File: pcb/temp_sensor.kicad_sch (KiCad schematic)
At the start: 4 parts, among them SW3 PTS810

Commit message: add top level schem and cleanup
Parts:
- removed C15: 100n, Capacitor_SMD:C_0402_1005Metric, symbol Device:C
- removed R7, R8: 10k, Resistor_SMD:R_0402_1005Metric, symbol Device:R
- removed SW3: PTS810, Button_Switch_SMD:SW_SPST_PTS810, symbol Switch:SW_SPST
- added C23: 0.1u, symbol Device:C
- added R39: 4.7k, symbol Device:R
- added U6: LM75ADP, symbol Sensor_Temperature:LM75B
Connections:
- net +3.3V: now also C23.1, R39.2, U6.8 (+Vs)
- net GND: now also C23.2, U6.4 (GND), U6.5 (A2), U6.6 (A1), U6.7 (A0)
- new net I2C.SCL: U6.2 (SCL)
- new net I2C.SDA: U6.1 (SDA)
- new net temp_int: R39.1, U6.3 (O.S.)
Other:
- company: RoboJackets Electrical Training -> (none)
- title: Debounced Button -> Temperature Sensor

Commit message: cleanup routing
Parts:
- removed R39: 4.7k, symbol Device:R
- added R12: 4.7k, symbol Device:R
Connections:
- net +3.3V: now also R12.1
- net temp_int: no longer names the net of U6.3 (O.S.)
- net temp_int: now also R12.2
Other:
- moved on the sheet: U6

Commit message: custom symbols for all ics
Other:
- note added: "Temperature Sensor"
- moved on the sheet: C23, R12, U6

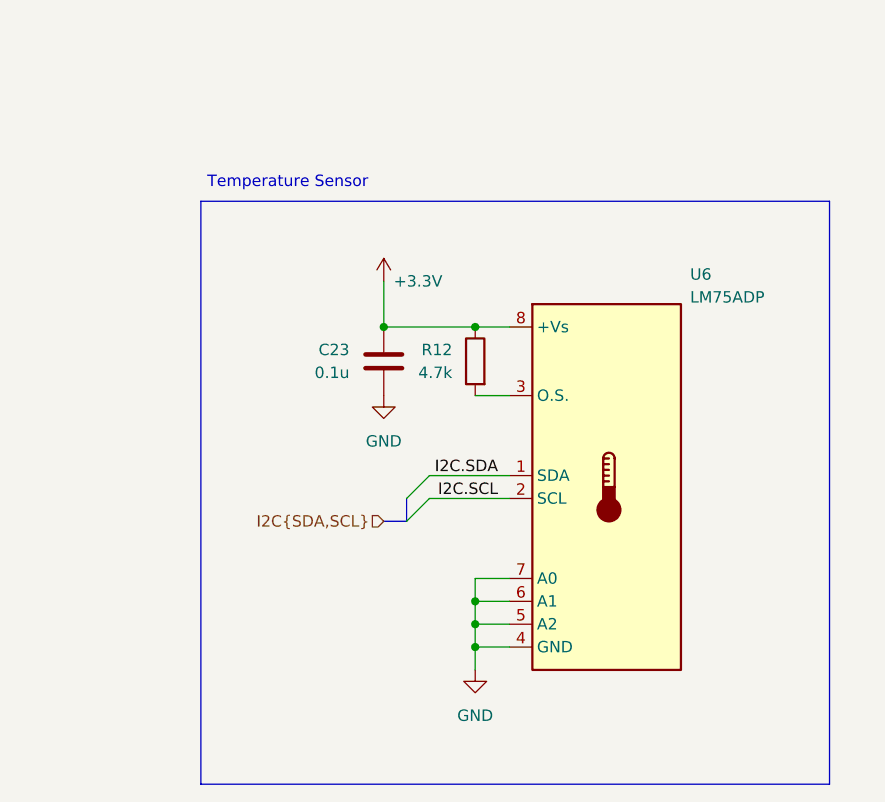
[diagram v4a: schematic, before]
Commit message: Adding some docs
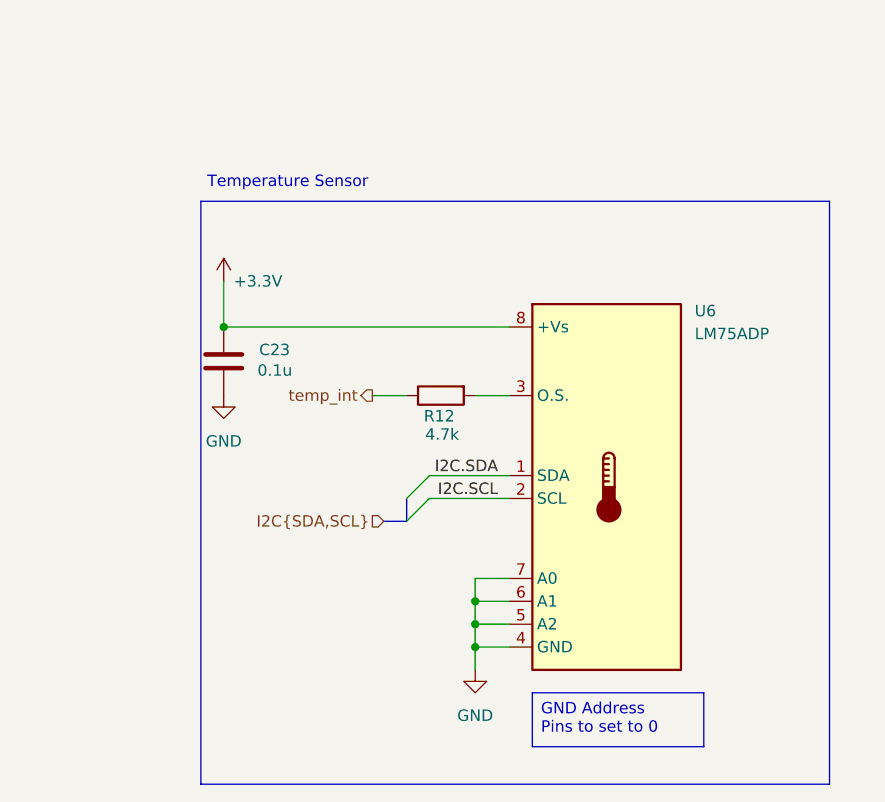
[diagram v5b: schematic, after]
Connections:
- net +3.3V: no longer R12.1
- new net temp_int: R12.1
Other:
- moved on the sheet: C23, R12

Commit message: Adding docs for GPIO and Color and removing INT
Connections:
- net temp_int is gone; now on net +3.3V: R12.1
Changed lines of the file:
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@@
 	(title_block
 		(title "Temperature Sensor")
-		(date "2026-10-27")
+		(date "2026-10-28")
+		(rev "2")
 	)
 	(rectangle
@@
 		)
 		(column_widths 21.59 30.48)
-		(row_heights 2.54 2.54 2.54 2.54 2.54 2.54 2.54)
+		(row_heights 2.54 2.54 2.54 2.54 2.54 2.54)
 		(cells
 			(table_cell "Device"
@@
 				(exclude_from_sim no)
 				(at 130.81 146.05 0)
-				(size 30.48 2.54)
-				(margins 0.9525 0.9525 0.9525 0.9525)
-				(span 1 1)
-				(fill
-					(type none)
-				)
-				(effects
-					(font
-						(size 1.27 1.27)
-					)
-					(justify left top)
-				)
-			)
-			(table_cell "Temp Int Pin"
-				(exclude_from_sim no)
-				(at 109.22 148.59 0)
-				(size 21.59 2.54)
-				(margins 0.9525 0.9525 0.9525 0.9525)
-				(span 1 1)
-				(fill
-					(type none)
-				)
-				(effects
-					(font
-						(size 1.27 1.27)
-					)
-					(justify left top)
-				)
-			)
-			(table_cell "RP2040 GPIO 1 (Pin 3)"
-				(exclude_from_sim no)
-				(at 130.81 148.59 0)
 				(size 30.48 2.54)
 				(margins 0.9525 0.9525 0.9525 0.9525)
@@
 			)
 			(justify right bottom)
-		)
-	)
-	(hierarchical_label "temp_int"
-		(shape output)
-		(at 128.27 87.63 180)
-		(effects
-			(font
-				(size 1.27 1.27)
-			)
-			(justify right)
 		)
 	)
@@
 					(unit 1)
 				)
+			)
+		)
+	)
+	(symbol
+		(lib_id "power:+3.3V")
+		(at 128.27 87.63 180)
+		(unit 1)
+		(body_style 1)
+		(exclude_from_sim no)
+		(in_bom yes)
+		(on_board yes)
+		(in_pos_files yes)
+		(dnp no)
+		(property "Reference" "#PWR074"
+			(at 128.27 83.82 0)
+			(hide yes)
+			(show_name no)
+			(do_not_autoplace no)
+			(effects
+				(font
+					(size 1.27 1.27)
+				)
+			)
+		)
+		(property "Value" "+3.3V"
+			(at 128.27 91.186 0)
+			(show_name no)
+			(do_not_autoplace no)
+			(effects
+				(font
+					(size 1.27 1.27)
+				)
+			)
+		)
+		(property "Footprint" ""
+			(at 128.27 87.63 0)
+			(hide yes)
+			(show_name no)
+			(do_not_autoplace no)
+			(effects
+				(font
+					(size 1.27 1.27)
+				)
+			)
+		)
+		(property "Datasheet" ""
+			(at 128.27 87.63 0)
+			(hide yes)
+			(show_name no)
+			(do_not_autoplace no)
+			(effects
+				(font
+					(size 1.27 1.27)
+				)
+			)
+		)
+		(property "Description" "Power symbol creates a global label with name \"+3.3V\""
+			(at 128.27 87.63 0)
+			(hide yes)
+			(show_name no)
+			(do_not_autoplace no)
+			(effects
+				(font
+					(size 1.27 1.27)
+				)
+			)
+		)
+		(pin "1"
+		)
+		(instances
+			(project "sensor_suite"
+				(path "/17df1232-b180-49eb-a49c-63e4861e42e5/f6c96202-8fec-4bb3-a83c-c3a8f09f5498"
+					(reference "#PWR074")
+					(unit 1)
+				)

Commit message: Slight clean up for HRM
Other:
- moved on the sheet: C23
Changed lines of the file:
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@@
 	)
 	(junction
-		(at 111.76 80.01)
+		(at 116.84 80.01)
 		(diameter 0)
 		(color 0 0 0 0)
@@
 	(wire
 		(pts
-			(xy 111.76 80.01) (xy 143.51 80.01)
-		)
-		(stroke
-			(width 0)
-			(type default)
-		)
-	)
-	(wire
-		(pts
-			(xy 111.76 74.93) (xy 111.76 80.01)
+			(xy 116.84 80.01) (xy 143.51 80.01)
+		)
+		(stroke
+			(width 0)
+			(type default)
+		)
+	)
+	(wire
+		(pts
+			(xy 116.84 74.93) (xy 116.84 80.01)
 		)
 		(stroke
@@
 	(symbol
 		(lib_id "Device:C")
-		(at 111.76 83.82 0)
+		(at 116.84 83.82 0)
 		(mirror y)
 		(unit 1)
@@
 		(dnp no)
 		(property "Reference" "C23"
-			(at 119.126 82.55 0)
+			(at 124.206 82.55 0)
 			(show_name no)
 			(do_not_autoplace no)
@@
 		)
 		(property "Value" "0.1u"
-			(at 119.38 84.836 0)
+			(at 124.46 84.836 0)
 			(show_name no)
 			(do_not_autoplace no)
@@
 		)
 		(property "Footprint" ""
-			(at 110.7948 87.63 0)
+			(at 115.8748 87.63 0)
 			(hide yes)
 			(show_name no)
@@
 		)
 		(property "Datasheet" "https://calchip.com/wp-content/uploads/2025/05/GMC-Series-3.pdf"
-			(at 111.76 83.82 0)
+			(at 116.84 83.82 0)
 			(hide yes)
 			(show_name no)
@@
 		)
 		(property "Description" "0.1 µF ±10% 16V Ceramic Capacitor X7R 0402 (1005 Metric)"
-			(at 111.76 83.82 0)
+			(at 116.84 83.82 0)
 			(hide yes)
 			(show_name no)
@@
 		)
 		(property "Manufactuer PN" "GMC04X7R104K16NT"
-			(at 111.76 83.82 0)
+			(at 116.84 83.82 0)
 			(hide yes)
 			(show_name no)
@@
 		)
 		(property "Vendor" "Digikey"
-			(at 111.76 83.82 0)
+			(at 116.84 83.82 0)
 			(hide yes)
 			(show_name no)
@@
 		)
 		(property "Vendor PN" "2571-GMC04X7R104K16NTTR-ND"
-			(at 111.76 83.82 0)
+			(at 116.84 83.82 0)
 			(hide yes)
 			(show_name no)
@@
 			)
 		)
+		(property "Manufactuer PN" ""
+			(at 154.94 97.79 0)
+			(hide yes)
+			(show_name no)
+			(do_not_autoplace no)
+			(effects
+				(font
+					(size 1.27 1.27)
+				)
+			)
+		)
+		(property "Vendor" ""
+			(at 154.94 97.79 0)
+			(hide yes)
+			(show_name no)
+			(do_not_autoplace no)
+			(effects
+				(font
+					(size 1.27 1.27)
+				)
+			)
+		)
+		(property "Vendor PN" ""
+			(at 154.94 97.79 0)
+			(hide yes)
+			(show_name no)
+			(do_not_autoplace no)
+			(effects
+				(font
+					(size 1.27 1.27)
+				)
+			)
+		)
 		(pin "2"
 		)
@@
 	(symbol
 		(lib_id "power:+3.3V")
-		(at 111.76 74.93 0)
+		(at 116.84 74.93 0)
 		(unit 1)
 		(body_style 1)
@@
 		(dnp no)
 		(property "Reference" "#PWR065"
-			(at 111.76 78.74 0)
+			(at 116.84 78.74 0)
 			(hide yes)
 			(show_name no)
@@
 		)
 		(property "Value" "+3.3V"
-			(at 115.57 74.93 0)
+			(at 120.65 74.93 0)
 			(show_name no)
 			(do_not_autoplace no)
@@
 		)
 		(property "Footprint" ""
-			(at 111.76 74.93 0)
+			(at 116.84 74.93 0)
 			(hide yes)
 			(show_name no)
@@
 		)
 		(property "Datasheet" ""
-			(at 111.76 74.93 0)
+			(at 116.84 74.93 0)
 			(hide yes)
 			(show_name no)
@@
 		)
 		(property "Description" "Power symbol creates a global label with name \"+3.3V\""
-			(at 111.76 74.93 0)
+			(at 116.84 74.93 0)
 			(hide yes)
 			(show_name no)
@@
 	(symbol
 		(lib_id "power:GND")
-		(at 111.76 87.63 0)
+		(at 116.84 87.63 0)
 		(unit 1)
 		(body_style 1)
@@
 		(fields_autoplaced yes)
 		(property "Reference" "#PWR066"
-			(at 111.76 93.98 0)
+			(at 116.84 93.98 0)
 			(hide yes)
 			(show_name no)
@@
 		)
 		(property "Value" "GND"
-			(at 111.76 92.71 0)
+			(at 116.84 92.71 0)
 			(show_name no)
 			(do_not_autoplace no)
@@
 		)
 		(property "Footprint" ""
-			(at 111.76 87.63 0)
+			(at 116.84 87.63 0)
 			(hide yes)
 			(show_name no)
@@
 		)
 		(property "Datasheet" ""
-			(at 111.76 87.63 0)
+			(at 116.84 87.63 0)
 			(hide yes)
 			(show_name no)
@@
 		)
 		(property "Description" "Power symbol creates a global label with name \"GND\" , ground"
-			(at 111.76 87.63 0)
-			(hide yes)
-			(show_name no)
+			(at 116.84 87.63 0)
+			(hide yes)
+			(show_name no)
